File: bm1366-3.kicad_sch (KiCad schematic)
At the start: 77 parts, among them U1 25MHz, U21 TLV3544, U23 AP7331, U24 AP7331, U25 BM1368_mode1, U27 BM1368_mode1

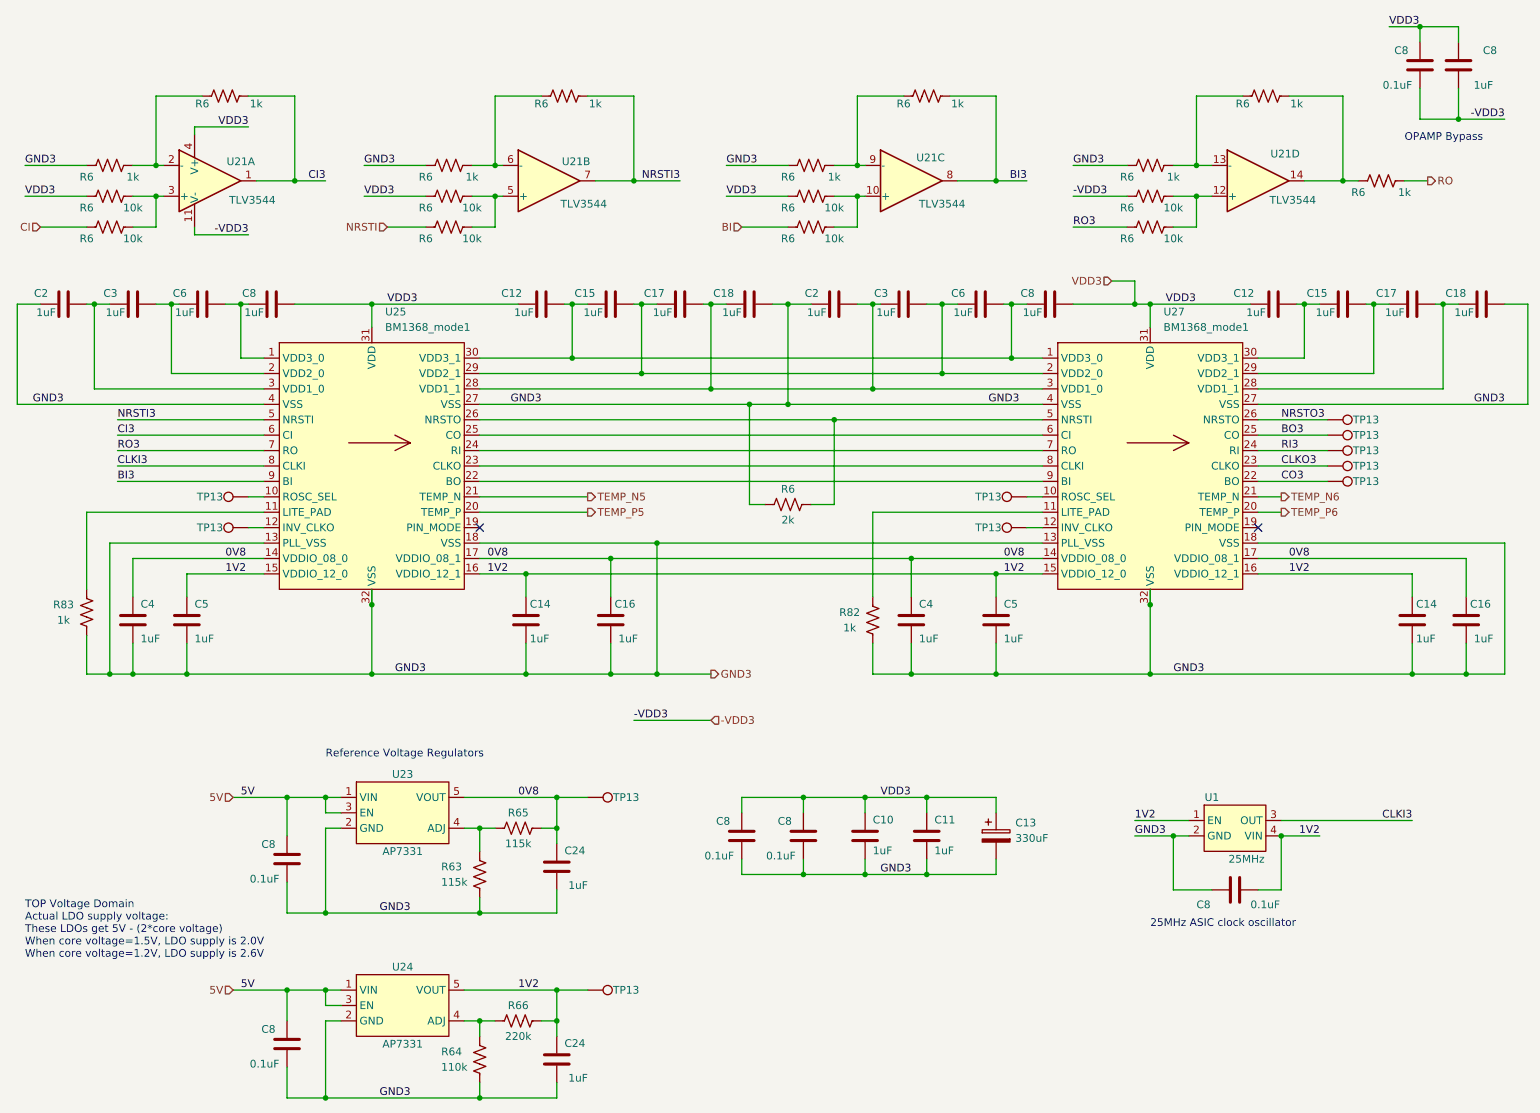
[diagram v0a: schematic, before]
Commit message: -Reset to 1V8/0V8 setup -Add TVS protection
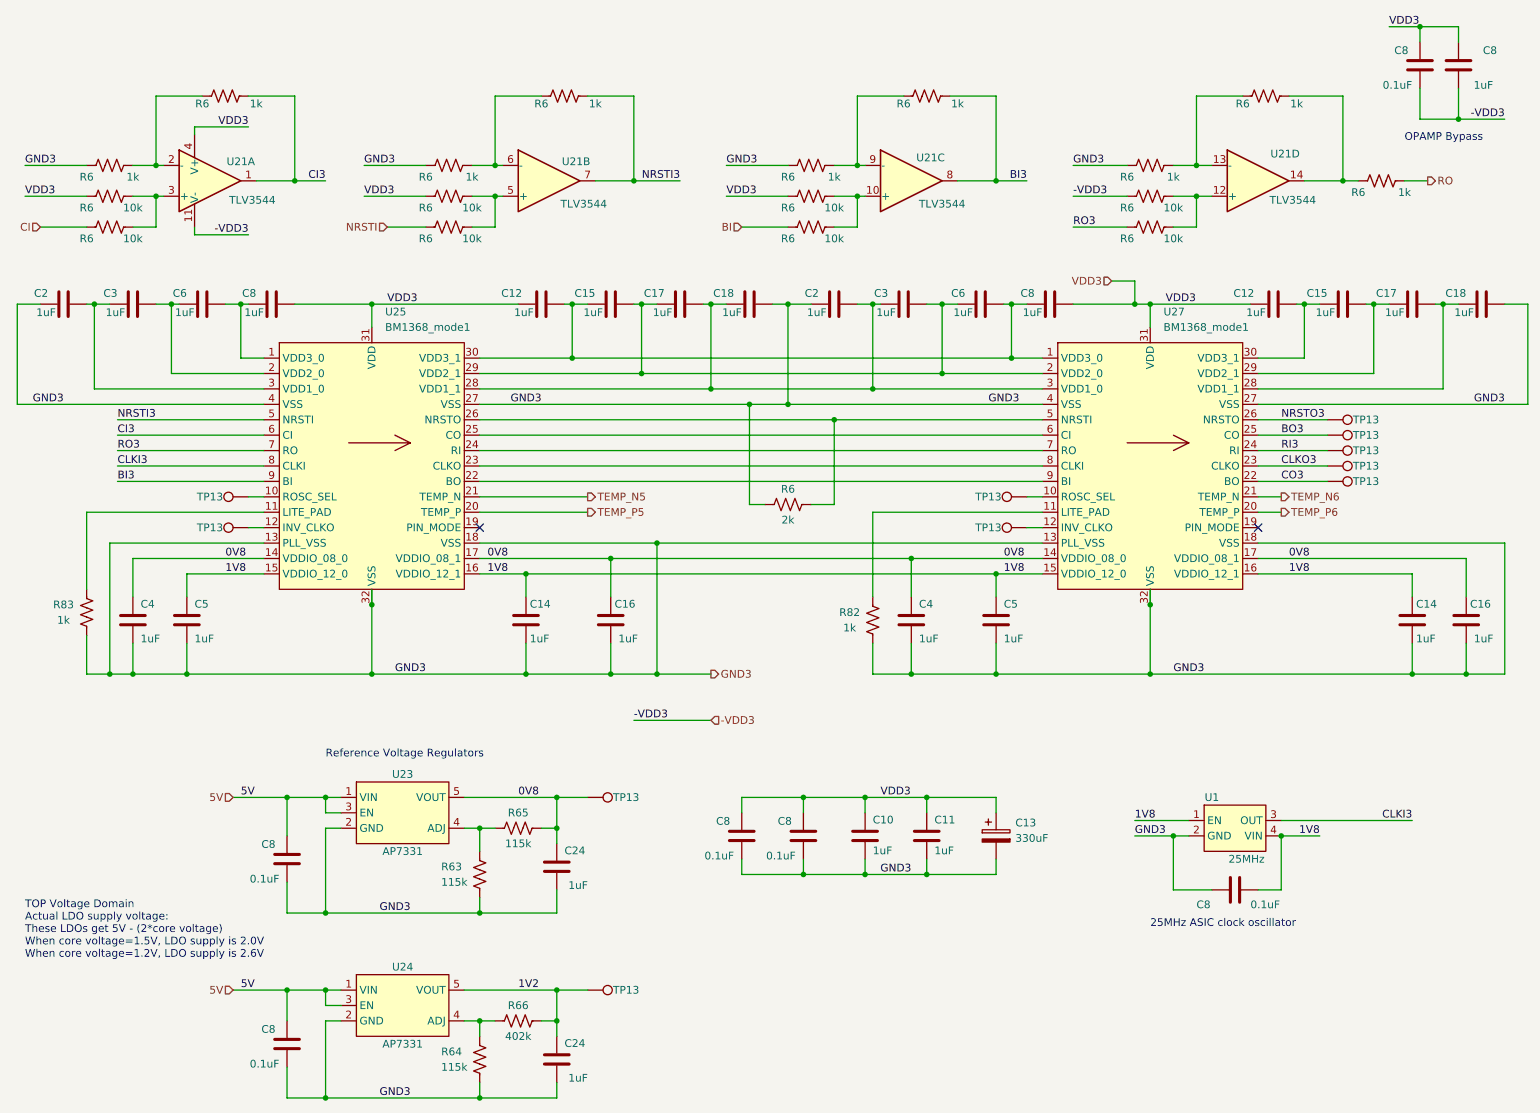
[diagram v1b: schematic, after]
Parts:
- R64: value 110k -> 115k; DK 311-110KLRTR-ND -> YAG2956CT-ND; PARTNO RC0402FR-07110KL -> RC0402FR-07115KL
- R66: value 220k -> 402k; DK 311-220KLRTR-ND -> YAG3151CT-ND; PARTNO RC0402FR-07220KL -> RC0402FR-07402KL
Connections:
- net 1V2: no longer C14.1, C14.1, C5.1, C5.1, C8.1, U1.1 (EN), U1.4 (VIN), U25.15 (VDDIO_12_0), U25.16 (VDDIO_12_1), U27.15 (VDDIO_12_0), U27.16 (VDDIO_12_1)
- new net 1V8: C14.1, C14.1, C5.1, C5.1, C8.1, U1.1 (EN), U1.4 (VIN), U25.15 (VDDIO_12_0), U25.16 (VDDIO_12_1), U27.15 (VDDIO_12_0), U27.16 (VDDIO_12_1)
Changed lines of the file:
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@@
 		)
 	)
-	(label "1V2"
+	(label "1V8"
 		(at 229.87 151.13 180)
 		(fields_autoplaced yes)
@@
 		)
 	)
-	(label "1V2"
+	(label "1V8"
 		(at 49.53 107.95 0)
 		(fields_autoplaced yes)
@@
 		)
 	)
-	(label "1V2"
+	(label "1V8"
 		(at 224.79 107.95 0)
 		(fields_autoplaced yes)
@@
 		)
 	)
-	(label "1V2"
+	(label "1V8"
 		(at 92.71 107.95 0)
 		(fields_autoplaced yes)
@@
 		)
 	)
-	(label "1V2"
+	(label "1V8"
 		(at 177.8 107.95 0)
 		(fields_autoplaced yes)
@@
 		)
 	)
-	(label "1V2"
+	(label "1V8"
 		(at 199.39 148.59 0)
 		(fields_autoplaced yes)
@@
 			)
 		)
-		(property "Value" "220k"
+		(property "Value" "402k"
 			(at 97.79 184.15 90)
 			(effects
@@
 			)
 		)
-		(property "DK" "311-220KLRTR-ND"
+		(property "DK" "YAG3151CT-ND"
 			(at 97.79 181.61 0)
 			(effects
@@
 			)
 		)
-		(property "PARTNO" "RC0402FR-07220KL"
+		(property "PARTNO" "RC0402FR-07402KL"
 			(at 97.79 181.61 0)
 			(effects
@@
 			)
 		)
-		(property "Value" "110k"
+		(property "Value" "115k"
 			(at 85.09 189.23 0)
 			(effects
@@
 			)
 		)
-		(property "DK" "311-110KLRTR-ND"
+		(property "DK" "YAG2956CT-ND"
 			(at 91.44 187.96 0)
 			(effects
@@
 			)
 		)
-		(property "PARTNO" "RC0402FR-07110KL"
+		(property "PARTNO" "RC0402FR-07115KL"
 			(at 91.44 187.96 0)
 			(effects

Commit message: updated to KiCad v9, filled in incomplete BOM and exported.
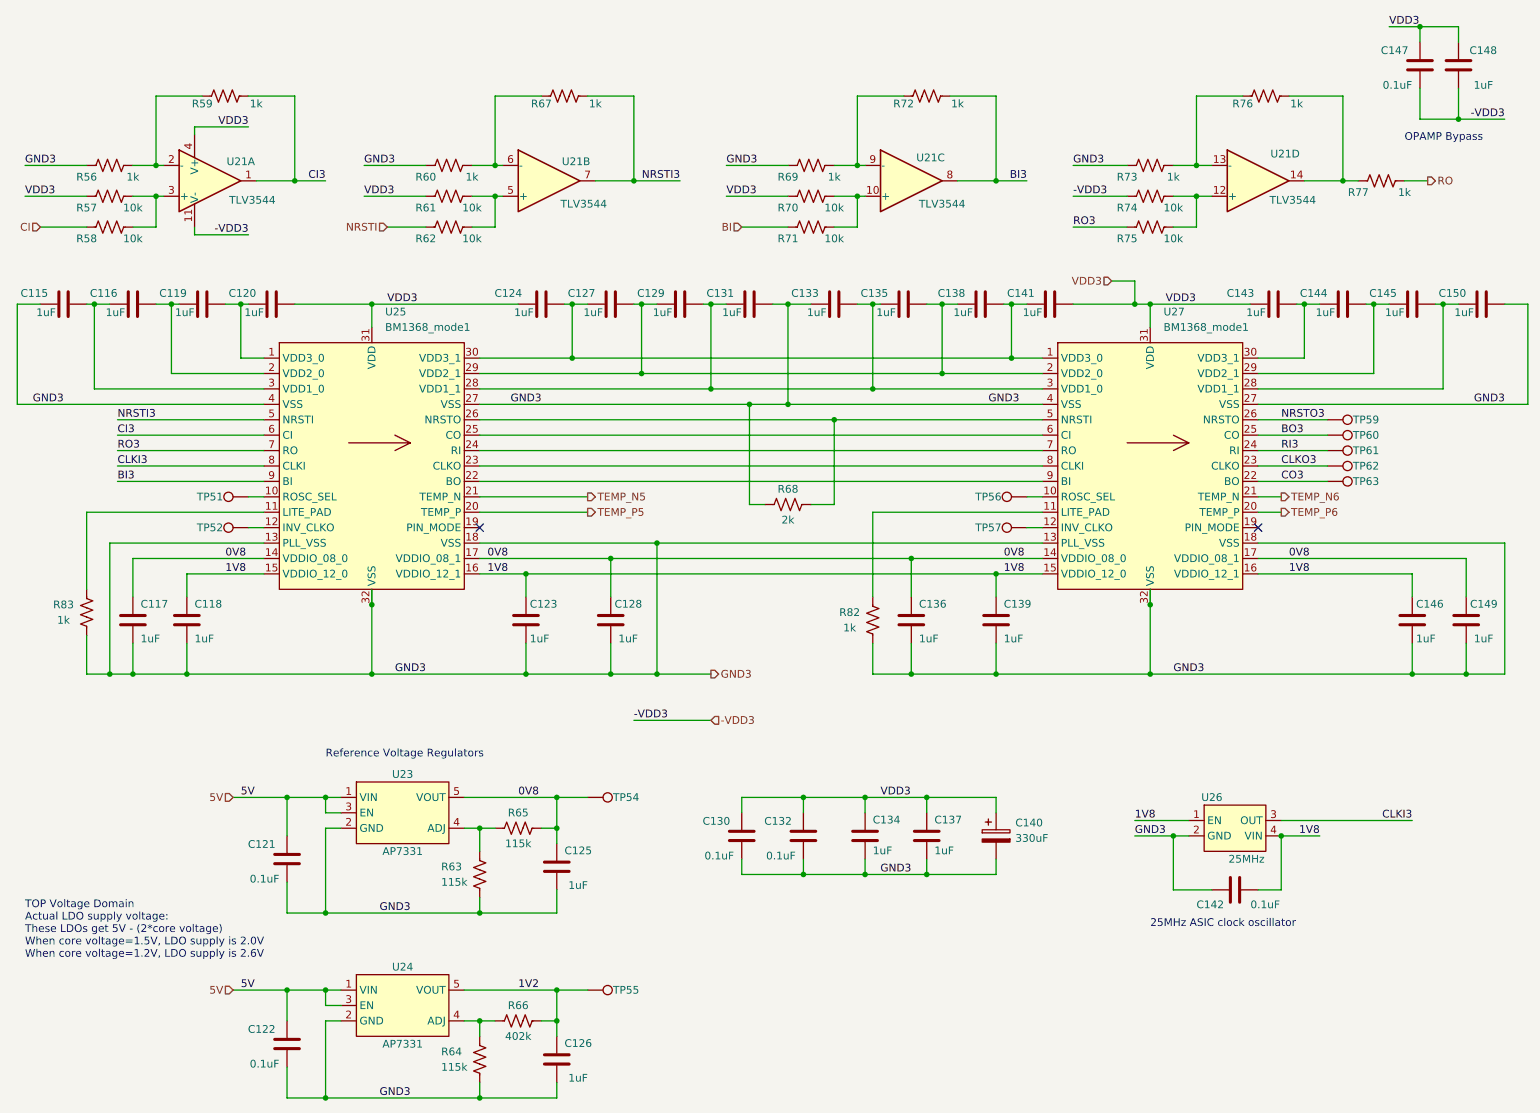
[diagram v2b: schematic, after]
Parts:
- renumbered C2 to C115, C3 to C116, C4 to C117, C5 to C118, C6 to C119, C8 to C120, C8 to C121, C8 to C122, C14 to C123, C12 to C124, C24 to C125, C24 to C126, C15 to C127, C16 to C128, C17 to C129, C8 to C130, C18 to C131, C8 to C132, C2 to C133, C10 to C134, C3 to C135, C4 to C136, C11 to C137, C6 to C138, C5 to C139, C13 to C140, C8 to C141, C8 to C142, C12 to C143, C15 to C144, C17 to C145, C14 to C146, C8 to C147, C8 to C148, C16 to C149, C18 to C150, R6 to R56, R6 to R57, R6 to R58, R6 to R59, R6 to R60, R6 to R61, R6 to R62, R6 to R67, R6 to R68, R6 to R69, R6 to R70, R6 to R71, R6 to R72, R6 to R73, R6 to R74, R6 to R75, R6 to R76, R6 to R77, TP13 to TP51, TP13 to TP52, TP13 to TP54, TP13 to TP55, TP13 to TP56, TP13 to TP57, TP13 to TP59, TP13 to TP60, TP13 to TP61, TP13 to TP62, TP13 to TP63, U1 to U26
